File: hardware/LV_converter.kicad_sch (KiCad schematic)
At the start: 28 parts, among them IC3 AP74502QTA8-7, J9 Conn_01x02, Q11 IRLML0030, Q4 NVMFWS1D7N04XMT1G, Q5 NVMFWS1D7N04XMT1G, U8 INA228

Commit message: major clean ups, fix LV enable labels, fixes and cleanup
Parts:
- removed R29, R30, R31: 10k, Resistor_SMD:R_0603_1608Metric_Pad0.98x0.95mm_HandSolder, symbol Device:R
- added D27: SMBJ33D, LV Carrier Library:SMBJ15DM3, symbol LV-Carrier:SMBJ15D-M3I
- added R23, R27, R28: 10k, Resistor_SMD:R_0603_1608Metric_Pad0.98x0.95mm_HandSolder, symbol Device:R
- C33: value 220n -> .1u
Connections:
- net +3V3: now also R28.1
- net GND: now also D27.1 (K); no longer Q11.2 (S)
- net LV_GND: now also Q11.2 (S), R27.2
- net VIN: now also D27.2 (A)
- net at Q11.1 (G): now also R23.2, R27.1
- net ALERT renamed SENSE_ALERT
- net DIODE_EN renamed PS_ENABLE
- net PS_ENABLE: now also R23.1
- net LV_PFAULT renamed LV_P_FAULT
- net LV_PROTECTED renamed LV_IN
- net LV_REGULATED renamed LV_24V_OUT
- net LV_SFAULT renamed LV_S_FAULT
- net SUPP_EN renamed PS_3V3_ENABLE
- net PS_3V3_ENABLE: now also R28.2
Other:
- note removed: "one set of 4.7k pull ups for I2C bus"
- moved on the sheet: C34, R20, R22

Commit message: more fix, clean up, add some debug led and testpoints
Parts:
- removed C28: 0.1u, symbol Device:C_Small
- added C47: 0.1u, symbol Device:C_Small
- added D20: LED, symbol Device:LED
- added R66: R, symbol Device:R
- added TP15: LV_24V_OUT, symbol Connector:TestPoint
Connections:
- net +3V3: now also C47.1
- net LV_24V_OUT: now also R66.1, TP15.1
- net LV_GND: now also C47.2, D20.1 (K)
- new net: D20.2 (A), R66.2
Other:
- note added: "ALERT pulls low on programmed fault"
- note added: "High Voltage 24V Ouput VIP Sensing"
- note added: "High Voltage DCDC Vicor"
- note added: "PC: referenced to HV_GND 5.7V when healthy pulls low on fault"
- note added: "Primary Control"
- note added: "SC: referenced to LV_GND 5.7V when healthy pulls low on fault"
- note added: "Secondary Control"
- note added: "place near VS"
- note removed: "Indicator LEDs"
- note removed: "Testpoints"
- moved on the sheet: C22, C23, C24, C26, C27, C31, C33, C34, C45, D27, IC3, J9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

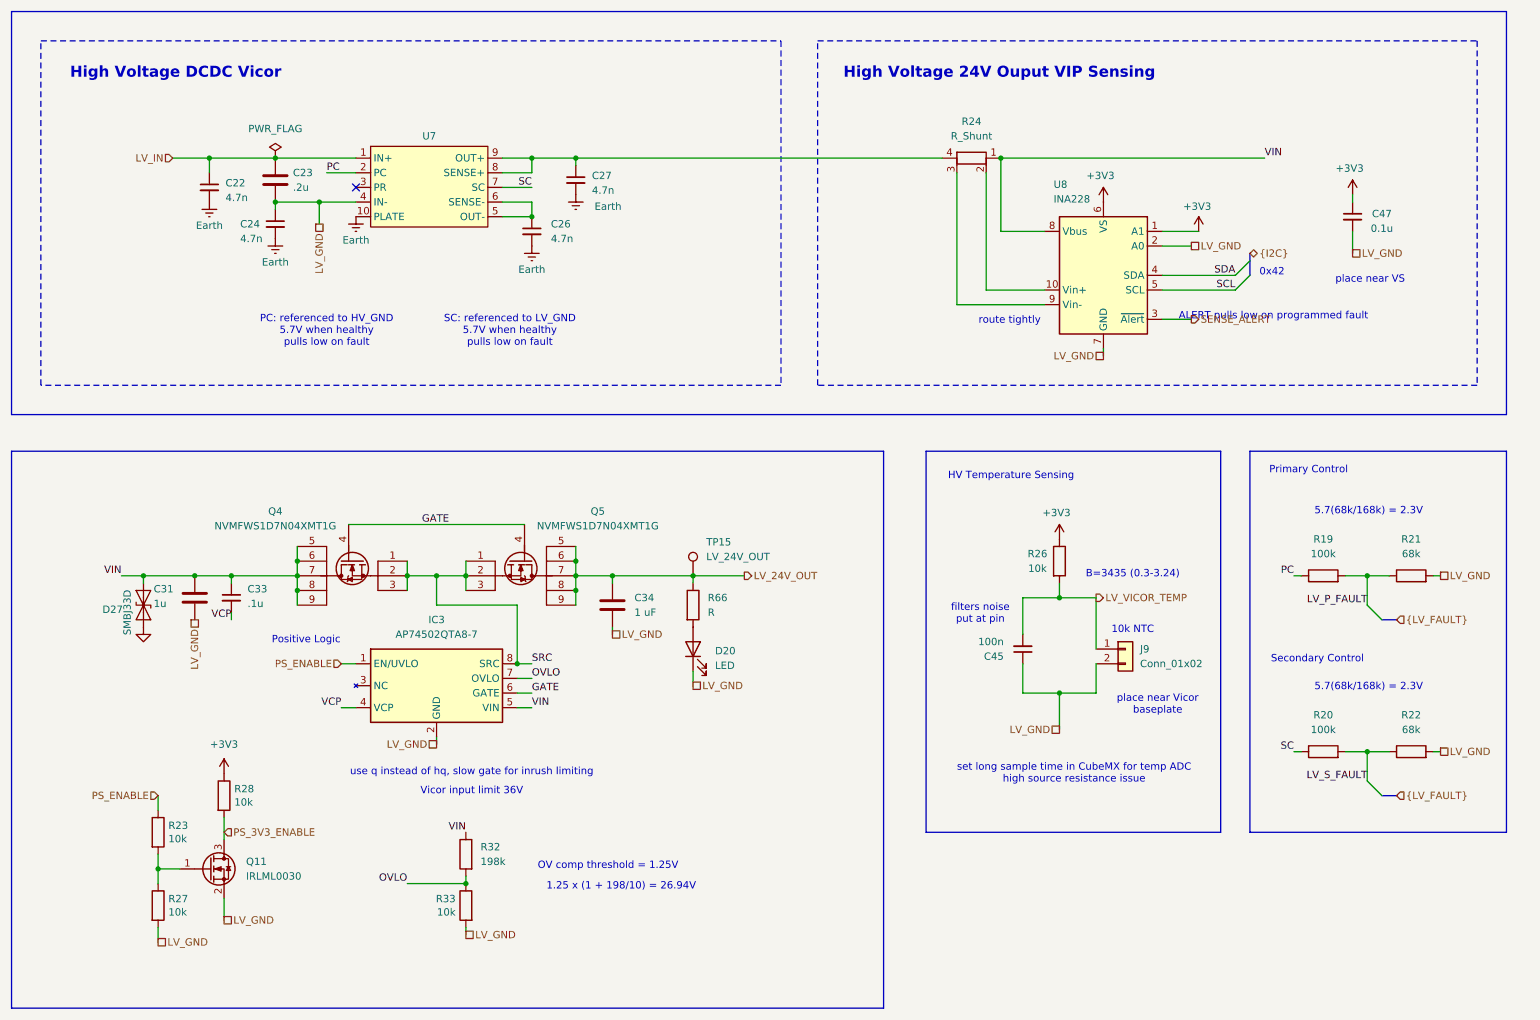
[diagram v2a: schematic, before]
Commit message: nearly all reviews addressed yippeeeeee
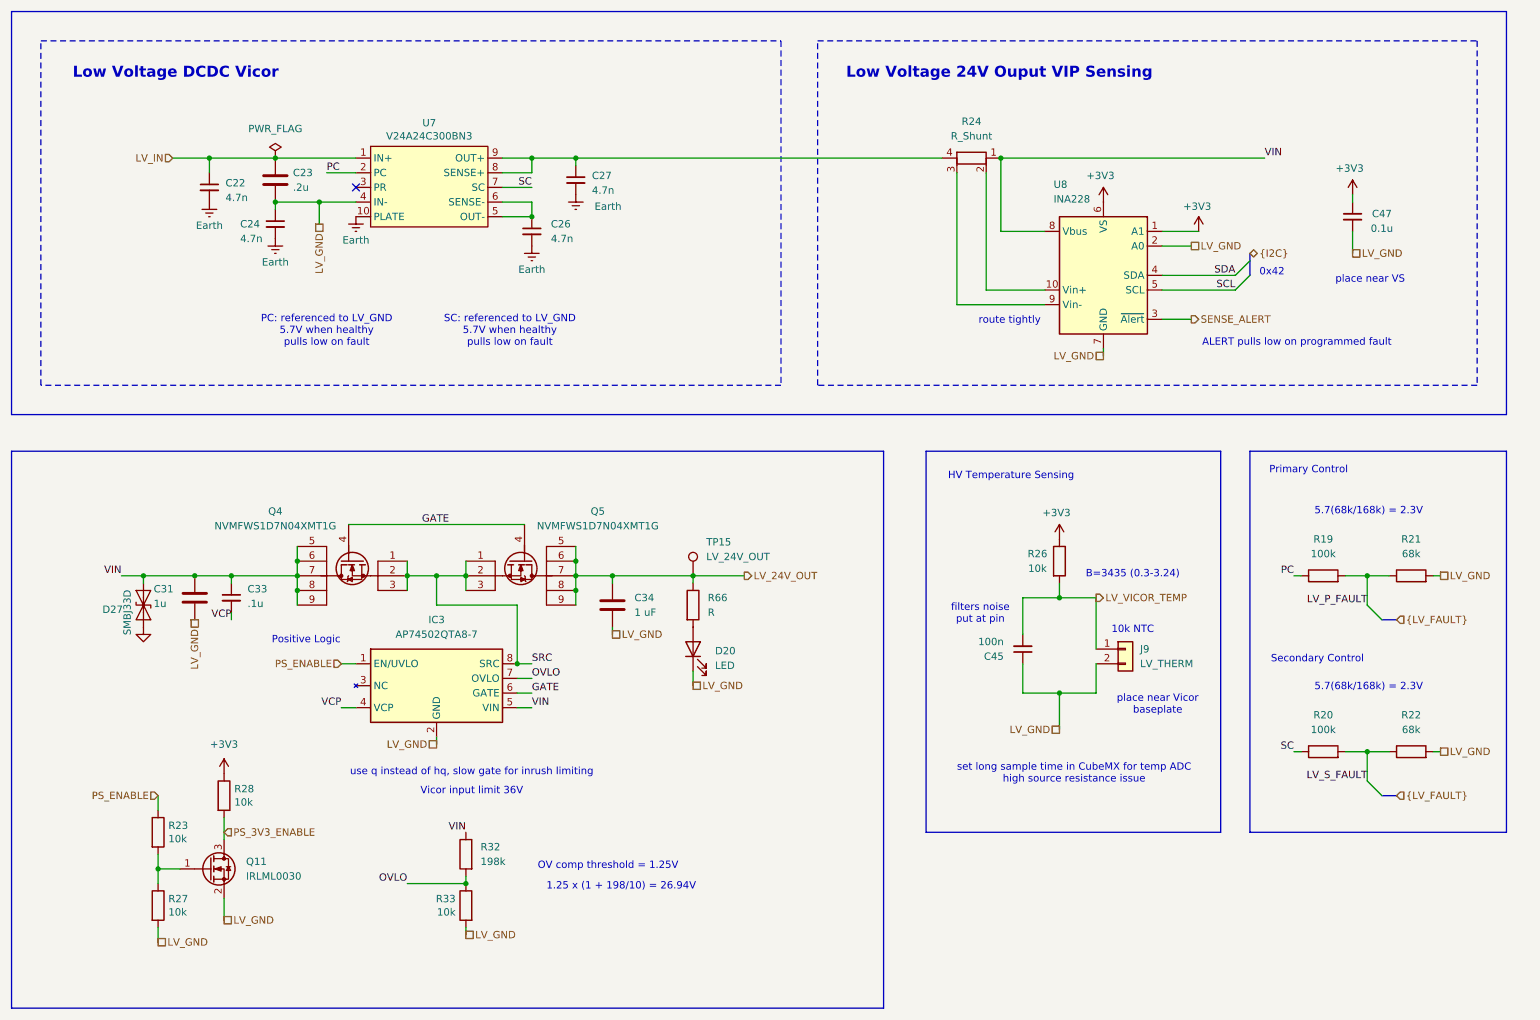
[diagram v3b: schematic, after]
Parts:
- J9: value Conn_01x02 -> LV_THERM
- U7: value (none) -> V24A24C300BN3
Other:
- note added: "Low Voltage 24V Ouput VIP Sensing"
- note added: "Low Voltage DCDC Vicor"
- note added: "PC: referenced to LV_GND 5.7V when healthy pulls low on fault"
- note removed: "High Voltage 24V Ouput VIP Sensing"
- note removed: "High Voltage DCDC Vicor"
- note removed: "PC: referenced to HV_GND 5.7V when healthy pulls low on fault"
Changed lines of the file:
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@@
 		)
 	)
-	(text "High Voltage 24V Ouput VIP Sensing"
+	(text "Low Voltage 24V Ouput VIP Sensing"
 		(exclude_from_sim no)
 		(at 190.246 29.718 0)
@@
 		)
 	)
-	(text "PC: referenced to HV_GND\n5.7V when healthy\npulls low on fault"
+	(text "PC: referenced to LV_GND\n5.7V when healthy\npulls low on fault"
 		(exclude_from_sim no)
 		(at 73.66 74.422 0)
@@
 	(text "ALERT pulls low on programmed fault"
 		(exclude_from_sim no)
-		(at 237.744 71.882 0)
+		(at 241.808 76.454 0)
 		(effects
 			(font
@@
 		)
 	)
-	(text "High Voltage DCDC Vicor"
+	(text "Low Voltage DCDC Vicor"
 		(exclude_from_sim no)
 		(at 47.498 29.718 0)
@@
 			)
 		)
-		(property "Value" "Conn_01x02"
+		(property "Value" "LV_THERM"
 			(at 214.63 132.0799 0)
 			(show_name no)
@@
 		(in_pos_files yes)
 		(dnp no)
-		(fields_autoplaced yes)
 		(property "Reference" "U7"
+			(at 91.44 38.354 0)
+			(show_name no)
+			(do_not_autoplace no)
+			(effects
+				(font
+					(size 1.27 1.27)
+				)
+			)
+		)
+		(property "Value" "V24A24C300BN3"
 			(at 91.44 40.64 0)
 			(show_name no)
-			(do_not_autoplace no)
-			(effects
-				(font
-					(size 1.27 1.27)
-				)
-			)
-		)
-		(property "Value" ""
-			(at 91.44 40.64 0)
-			(show_name no)

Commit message: done all obbb specific reviews beside indicator led resistor values + math, goodnight
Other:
- note added: "B=3435"
- note added: "Expected: 20-100°C → 1.81V to 0.30V"
- note removed: "B=3435 (0.3-3.24)"
- moved on the sheet: C45, J9, Q11, R23, R26, R27, R28, R32, R33

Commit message: fixes only thing left is finish assigning footprints, its frozen
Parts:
- C26: renamed from C31; LCSC P/N (none) -> C15849; Mouser P/N (none) -> MLASU063SB7102KFNA01 MLASU168SB5105KTNA01
- C27: renamed from C22; footprint (none) -> Capacitor_SMD:C_0603_1608Metric_Pad1.08x0.95mm_HandSolder; LCSC P/N (none) -> C106218; Mouser P/N (none) -> 06035C472K4T2A
- C28: renamed from C33; value .1u -> 0.1u; footprint (none) -> Capacitor_SMD:C_0603_1608Metric_Pad1.08x0.95mm_HandSolder; LCSC P/N (none) -> C14663; Mouser P/N (none) -> MLASH168SB7104KTNA01
- C29: renamed from C23; footprint (none) -> Capacitor_SMD:C_0603_1608Metric_Pad1.08x0.95mm_HandSolder
- C30: renamed from C24; footprint (none) -> Capacitor_SMD:C_0603_1608Metric_Pad1.08x0.95mm_HandSolder; LCSC P/N (none) -> C106218; Mouser P/N (none) -> 06035C472K4T2A
- C31: renamed from C26; footprint (none) -> Capacitor_SMD:C_0603_1608Metric_Pad1.08x0.95mm_HandSolder; LCSC P/N (none) -> C106218; Mouser P/N (none) -> 06035C472K4T2A
- C32: renamed from C27; footprint (none) -> Capacitor_SMD:C_0603_1608Metric_Pad1.08x0.95mm_HandSolder; LCSC P/N (none) -> C106218; Mouser P/N (none) -> 06035C472K4T2A
- C33: renamed from C34; value 1 uF -> 1u; LCSC P/N (none) -> C15849; Mouser P/N (none) -> MLASU063SB7102KFNA01 MLASU168SB5105KTNA01
- C34: renamed from C45; footprint (none) -> Capacitor_SMD:C_0603_1608Metric_Pad1.08x0.95mm_HandSolder; LCSC P/N (none) -> C14663; Mouser P/N (none) -> MLASH168SB7104KTNA01
- C35: renamed from C47; footprint (none) -> Capacitor_SMD:C_0603_1608Metric_Pad1.08x0.95mm_HandSolder; LCSC P/N (none) -> C14663; Mouser P/N (none) -> MLASH168SB7104KTNA01
- D10: renamed from D20; value LED -> LV24V_LED; footprint (none) -> LED_SMD:LED_0603_1608Metric_Pad1.05x0.95mm_HandSolder
- D9: renamed from D27; footprint LV Carrier Library:SMBJ15DM3 -> OBBB Footprints:SMBJ15DM3; LCSC P/N (none) -> C78419
- IC2: renamed from IC3; footprint LV Carrier Library:AP74502HQTA87 -> OBBB Footprints:AP74502HQTA87; LCSC P/N (none) -> C48989247
- J6: renamed from J9; footprint (none) -> LHRS_Connectors:105313-2102
- Q5: renamed from Q11; LCSC P/N (none) -> C67272
- Q6: renamed from Q4; footprint LV Carrier Library:NVMFWS3D0P04M8LT1G -> OBBB Footprints:NVMFWS3D0P04M8LT1G; LCSC P/N (none) -> C133142
- Q7: renamed from Q5; footprint LV Carrier Library:NVMFWS3D0P04M8LT1G -> OBBB Footprints:NVMFWS3D0P04M8LT1G; LCSC P/N (none) -> C133142
- R44: renamed from R66; value R -> 22k
- renumbered R28 to R39, R23 to R40, R27 to R41, R32 to R42, R33 to R43, R24 to R45, R26 to R46, R19 to R47, R20 to R48, R21 to R49, R22 to R50, TP15 to TP11, U7 to U8, U8 to U9
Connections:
- net LV_P_FAULT renamed LV_PC_FAULT
- net LV_S_FAULT renamed LV_SC_FAULT

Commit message: switching branches
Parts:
- R39, R40, R41, R43: LCSC P/N (none) -> C25804
- R42: LCSC P/N (none) -> C1693952
- R44: footprint (none) -> Resistor_SMD:R_0603_1608Metric_Pad0.98x0.95mm_HandSolder; LCSC P/N (none) -> C31850
- R46: footprint (none) -> Resistor_SMD:R_0603_1608Metric_Pad0.98x0.95mm_HandSolder; LCSC P/N (none) -> C25804
- R47, R48: footprint (none) -> Resistor_SMD:R_0603_1608Metric_Pad0.98x0.95mm_HandSolder; LCSC P/N (none) -> C25803
- R49, R50: footprint (none) -> Resistor_SMD:R_0603_1608Metric_Pad0.98x0.95mm_HandSolder; LCSC P/N (none) -> C177284
- TP11: footprint (none) -> TestPoint:TestPoint_THTPad_D3.0mm_Drill1.5mm
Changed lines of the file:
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@@
 		)
 	)
-	(text "Expected: 20-100°C → 1.81V to 0.30V"
-		(exclude_from_sim no)
-		(at 54.864 122.682 0)
-		(effects
-			(font
-				(size 1.27 1.27)
-			)
-		)
-	)
 	(text "SC: referenced to LV_GND\n5.7V when healthy\npulls low on fault"
 		(exclude_from_sim no)
@@
 			)
 		)
+		(property "LCSC P/N" "C25804"
+			(at 60.325 166.37 0)
+			(hide yes)
+			(show_name no)
+			(do_not_autoplace no)
+			(effects
+				(font
+					(size 1.27 1.27)
+				)
+			)
+		)
 		(pin "1"
 		)
@@
 			)
 		)
-		(property "Footprint" ""
+		(property "Footprint" "Resistor_SMD:R_0603_1608Metric_Pad0.98x0.95mm_HandSolder"
 			(at 261.62 149.098 90)
 			(hide yes)
@@
 			)
 		)
+		(property "LCSC P/N" "C177284"
+			(at 261.62 147.32 90)
+			(hide yes)
+			(show_name no)
+			(do_not_autoplace no)
+			(effects
+				(font
+					(size 1.27 1.27)
+				)
+			)
+		)
 		(pin "1"
 		)
@@
 			)
 		)
+		(property "LCSC P/N" "C25804"
+			(at 93.98 179.07 0)
+			(hide yes)
+			(show_name no)
+			(do_not_autoplace no)
+			(effects
+				(font
+					(size 1.27 1.27)
+				)
+			)
+		)
 		(pin "1"
 		)
@@
 			)
 		)
-		(property "Footprint" ""
+		(property "Footprint" "TestPoint:TestPoint_THTPad_D3.0mm_Drill1.5mm"
 			(at 142.24 116.84 0)
 			(hide yes)
@@
 			)
 		)
-		(property "Footprint" ""
+		(property "Footprint" "Resistor_SMD:R_0603_1608Metric_Pad0.98x0.95mm_HandSolder"
 			(at 246.38 149.098 90)
 			(hide yes)
@@
 			)
 		)
+		(property "LCSC P/N" "C25803"
+			(at 246.38 147.32 90)
+			(hide yes)
+			(show_name no)
+			(do_not_autoplace no)
+			(effects
+				(font
+					(size 1.27 1.27)
+				)
+			)
+		)
 		(pin "1"
 		)
@@
 			)
 		)
-		(property "Footprint" ""
+		(property "Footprint" "Resistor_SMD:R_0603_1608Metric_Pad0.98x0.95mm_HandSolder"
 			(at 135.382 121.92 90)
 			(hide yes)
@@
 			)
 		)
+		(property "LCSC P/N" "C31850"
+			(at 137.16 121.92 0)
+			(hide yes)
+			(show_name no)
+			(do_not_autoplace no)
+			(effects
+				(font
+					(size 1.27 1.27)
+				)
+			)
+		)
 		(pin "1"
 		)
@@
 			)
 		)
-		(property "Footprint" ""
+		(property "Footprint" "Resistor_SMD:R_0603_1608Metric_Pad0.98x0.95mm_HandSolder"
 			(at 198.882 119.38 90)
 			(hide yes)
@@
 			)
 		)
+		(property "LCSC P/N" "C25804"
+			(at 200.66 119.38 0)
+			(hide yes)
+			(show_name no)
+			(do_not_autoplace no)
+			(effects
+				(font
+					(size 1.27 1.27)
+				)
+			)
+		)
 		(pin "1"
 		)
@@
 			)
 		)
-		(property "Footprint" ""
+		(property "Footprint" "Resistor_SMD:R_0603_1608Metric_Pad0.98x0.95mm_HandSolder"
 			(at 246.38 118.618 90)
 			(hide yes)
@@
 			)
 		)
+		(property "LCSC P/N" "C25803"
+			(at 246.38 116.84 90)
+			(hide yes)
+			(show_name no)
+			(do_not_autoplace no)
+			(effects
+				(font
+					(size 1.27 1.27)
+				)
+			)
+		)
 		(pin "1"
 		)
@@
 			)
 		)
+		(property "LCSC P/N" "C25804"
+			(at 43.815 160.02 0)
+			(hide yes)
+			(show_name no)
+			(do_not_autoplace no)
+			(effects
+				(font
+					(size 1.27 1.27)
+				)
+			)
+		)
 		(pin "1"
 		)
@@
 			)
 		)
+		(property "LCSC P/N" "C25804"
+			(at 60.325 179.07 0)
+			(hide yes)
+			(show_name no)
+			(do_not_autoplace no)
+			(effects
+				(font
+					(size 1.27 1.27)
+				)
+			)
+		)
 		(pin "1"
 		)
@@
 			)
 		)
+		(property "LCSC P/N" "C1693952"
+			(at 93.98 170.18 0)
+			(hide yes)
+			(show_name no)
+			(do_not_autoplace no)
+			(effects
+				(font
+					(size 1.27 1.27)
+				)
+			)
+		)
 		(pin "2"
 		)
@@
 			)
 		)
-		(property "Footprint" ""
+		(property "Footprint" "Resistor_SMD:R_0603_1608Metric_Pad0.98x0.95mm_HandSolder"
 			(at 261.62 118.618 90)
 			(hide yes)
@@
 			(hide yes)
 			(show_name no)
+			(do_not_autoplace no)
+			(effects
+				(font
+					(size 1.27 1.27)
+				)
+			)
+		)
+		(property "LCSC P/N" "C177284"
+			(at 261.62 116.84 90)
+			(hide yes)
+			(show_name no)

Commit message: switched out ina228 for hall
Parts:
- removed C35: 0.1u, Capacitor_SMD:C_0603_1608Metric_Pad1.08x0.95mm_HandSolder, symbol Device:C_Small
- removed R45: R_Shunt, symbol Device:R_Shunt
- removed U9: INA228, Package_SO:TSSOP-10_3x3mm_P0.5mm, symbol Sensor_Energy:INA228
- added C79: 100n, symbol Device:C_Small
- added C80: 0.1n, Capacitor_SMD:C_0603_1608Metric_Pad1.08x0.95mm_HandSolder, symbol Device:C_Small
- added R109: 10k, Resistor_SMD:R_0603_1608Metric_Pad0.98x0.95mm_HandSolder, symbol Device:R
- added R110: 1k, Resistor_SMD:R_0603_1608Metric_Pad0.98x0.95mm_HandSolder, symbol Device:R
- added TP25: LV_OUT_V, symbol Connector:TestPoint
- added U17: TMCS1107A2UQDR, OBBB Footprints:TMCS1107A3BQDR, symbol OBBB Symbols:TMCS1107A3BQDR
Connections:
- net LV_GND: now also C79.2, C80.1, R110.2, U17.5 (GND), U17.6 (NC)
- net VIN: now also U17.3 (IN-), U17.4 (IN-)
- net IN+: now reaches C32.1, U8.8 (SENSE+), U8.9 (OUT+)
- net IN+: now also R109.1, U17.1 (IN+), U17.2 (IN+)
- new net LV_OUT_I: U17.7 (VOUT)
- new net LV_OUT_V: C79.1, R109.2, R110.1, TP25.1
- new net VS: C80.2, U17.8 (VS)
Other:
- note added: "3A: .33 + 3x0.15 = 0.78V VOUT"
- note added: "pick TMCS1107A1B/U-A3B/U variant for 3.3V supply voltage recommended: TMCS1107A3U"
- note removed: "0x42"
- note removed: "ALERT pulls low on programmed fault"
- note removed: "place near VS"
- note removed: "route tightly"
- moved on the sheet: C27, C29, C30, C31, C32, U8
